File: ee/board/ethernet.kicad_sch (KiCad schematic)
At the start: 20 parts, among them J8 HR911105A, U1 RTL8201F, Y1 Crystal_GND24_Small

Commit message: Nearly finished routing.
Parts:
- removed RN1 (x2): 10k, Resistor_SMD:R_Array_Convex_4x0402, symbol Device:R_Pack04
- added C16: 100nF, Capacitor_SMD:C_0603_1608Metric, symbol Device:C_Small
- added R17 (x7): 5.1k, Resistor_SMD:R_0603_1608Metric, symbol Device:R_Small_US
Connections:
- net +3V3: now also C16.1, R17.2, R17.2, R17.2, R17.2
- net GND: now also C16.2, R17.1, R17.1, R17.1
- net RMII_MDC: now also R17.1
- net RMII_MDIO: now also R17.1
- net RMII_RXD1: now also R17.2
- net RMII_RXER: now also R17.2
- net at U1.12 (CLK_CTL): now also R17.1, R17.2
- net at U1.8 (RXDV): now also R17.1
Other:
- moved on the sheet: C10, C8

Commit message: Finished R1
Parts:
- C10, C11, C12, C16, C8: MPN (none) -> CC0603KRX7R7BB104
- C14, C15: MPN (none) -> CC0603JPNPO9BN180
- R17: MPN (none) -> RC0603FR-135K1L
- R17: MPN (none) -> RC0603FR-13470KL
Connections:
- net GND: now also J8.13 (SHIELD), J8.14 (SHIELD); no longer J8.15 (SHIELD), J8.16 (SHIELD)
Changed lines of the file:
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@@
   (junction (at 86.995 90.17) (diameter 0) (color 0 0 0 0)
+  )
+  (junction (at 190.5 124.46) (diameter 0) (color 0 0 0 0)
   )
   (junction (at 83.185 100.33) (diameter 0) (color 0 0 0 0)
@@
     (stroke (width 0) (type default))
   )
+  (wire (pts (xy 190.5 121.92) (xy 190.5 124.46))
+    (stroke (width 0) (type default))
+  )
   (wire (pts (xy 181.61 92.71) (xy 185.42 92.71))
     (stroke (width 0) (type default))
@@
     (stroke (width 0) (type default))
   )
+  (wire (pts (xy 190.5 124.46) (xy 191.77 124.46))
+    (stroke (width 0) (type default))
+  )
   (wire (pts (xy 137.795 88.265) (xy 145.415 88.265))
     (stroke (width 0) (type default))
@@
     (stroke (width 0) (type default))
   )
-  (wire (pts (xy 190.5 125.095) (xy 190.5 123.19))
+  (wire (pts (xy 190.5 129.54) (xy 190.5 124.46))
     (stroke (width 0) (type default))
   )
@@
     (stroke (width 0) (type default))
   )
+  (wire (pts (xy 191.77 121.92) (xy 190.5 121.92))
+    (stroke (width 0) (type default))
+  )
   (wire (pts (xy 69.215 109.855) (xy 69.215 116.84))
     (stroke (width 0) (type default))
@@
   )
   (wire (pts (xy 137.795 74.295) (xy 145.415 74.295))
-    (stroke (width 0) (type default))
-  )
-  (wire (pts (xy 190.5 123.19) (xy 191.77 123.19))
     (stroke (width 0) (type default))
   )
@@
     (pin "11")
     (pin "12")
-    (pin "15")
-    (pin "16")
     (pin "2")
     (pin "3")
@@
     (pin "8")
     (pin "9")
+    (pin "13")
+    (pin "14")
     (instances
       (project "board"
@@
     )
     (property "Datasheet" "~" (at 173.99 124.46 0)
+      (effects (font (size 1.27 1.27)) hide)
+    )
+    (property "MPN" "RC0603FR-135K1L" (at 173.99 124.46 0)
       (effects (font (size 1.27 1.27)) hide)
     )
@@
     )
   )
-  (symbol (lib_id "power:GND") (at 190.5 125.095 0) (unit 1)
+  (symbol (lib_id "power:GND") (at 190.5 129.54 0) (unit 1)
     (in_bom yes) (on_board yes) (dnp no) (fields_autoplaced)
-    (property "Reference" "#PWR030" (at 190.5 131.445 0)
-      (effects (font (size 1.27 1.27)) hide)
-    )
-    (property "Value" "GND" (at 190.5 129.5384 0)
-      (effects (font (size 1.27 1.27)) hide)
-    )
-    (property "Footprint" "" (at 190.5 125.095 0)
-      (effects (font (size 1.27 1.27)) hide)
-    )
-    (property "Datasheet" "" (at 190.5 125.095 0)
+    (property "Reference" "#PWR030" (at 190.5 135.89 0)
+      (effects (font (size 1.27 1.27)) hide)
+    )
+    (property "Value" "GND" (at 190.5 133.9834 0)
+      (effects (font (size 1.27 1.27)) hide)
+    )
+    (property "Footprint" "" (at 190.5 129.54 0)
+      (effects (font (size 1.27 1.27)) hide)
+    )
+    (property "Datasheet" "" (at 190.5 129.54 0)
       (effects (font (size 1.27 1.27)) hide)
     )
@@
       (effects (font (size 1.27 1.27)) hide)
     )
+    (property "MPN" "CC0603KRX7R7BB104" (at 154.305 40.005 0)
+      (effects (font (size 1.27 1.27)) hide)
+    )
     (pin "1")
     (pin "2")
@@
       (effects (font (size 1.27 1.27)) hide)
     )
+    (property "MPN" "CC0603JPNPO9BN180" (at 154.94 85.09 0)
+      (effects (font (size 1.27 1.27)) hide)
+    )
     (pin "1")
     (pin "2")
@@
     )
     (property "Datasheet" "~" (at 182.245 118.11 0)
+      (effects (font (size 1.27 1.27)) hide)
+    )
+    (property "MPN" "RC0603FR-13470KL" (at 182.245 118.11 90)
       (effects (font (size 1.27 1.27)) hide)
     )
@@
     )
     (property "Datasheet" "~" (at 132.715 40.005 0)
+      (effects (font (size 1.27 1.27)) hide)
+    )
+    (property "MPN" "CC0603KRX7R7BB104" (at 132.715 40.005 0)
       (effects (font (size 1.27 1.27)) hide)
     )
@@
       (effects (font (size 1.27 1.27)) hide)
     )
+    (property "MPN" "RC0603FR-135K1L" (at 128.905 74.93 90)
+      (effects (font (size 1.27 1.27)) hide)
+    )
     (pin "1")
     (pin "2")
@@
     )
     (property "Datasheet" "~" (at 173.99 98.425 0)
+      (effects (font (size 1.27 1.27)) hide)
+    )
+    (property "MPN" "RC0603FR-135K1L" (at 173.99 98.425 0)
       (effects (font (size 1.27 1.27)) hide)
     )
@@
       (effects (font (size 1.27 1.27)) hide)
     )
+    (property "MPN" "RC0603FR-135K1L" (at 92.075 48.895 0)
+      (effects (font (size 1.27 1.27)) hide)
+    )
     (pin "1")
     (pin "2")
@@
       (effects (font (size 1.27 1.27)) hide)
     )
+    (property "MPN" "RC0603FR-135K1L" (at 76.2 48.26 0)
+      (effects (font (size 1.27 1.27)) hide)
+    )
     (pin "1")
     (pin "2")
@@
     )
     (property "Datasheet" "~" (at 130.81 99.695 0)
+      (effects (font (size 1.27 1.27)) hide)
+    )
+    (property "MPN" "CC0603KRX7R7BB104" (at 130.81 99.695 0)
       (effects (font (size 1.27 1.27)) hide)
     )
@@
       (effects (font (size 1.27 1.27)) hide)
     )
+    (property "MPN" "RC0603FR-135K1L" (at 76.2 106.68 0)
+      (effects (font (size 1.27 1.27)) hide)
+    )
     (pin "1")
     (pin "2")
@@
       (effects (font (size 1.27 1.27)) hide)
     )
+    (property "MPN" "CC0603JPNPO9BN180" (at 154.94 77.47 0)
+      (effects (font (size 1.27 1.27)) hide)
+    )
     (pin "1")
     (pin "2")
@@
       (effects (font (size 1.27 1.27)) hide)
     )
+    (property "MPN" "CC0603KRX7R7BB104" (at 142.875 40.005 0)
+      (effects (font (size 1.27 1.27)) hide)
+    )
     (pin "1")
     (pin "2")
@@
     )
     (property "Datasheet" "~" (at 83.185 106.68 0)
+      (effects (font (size 1.27 1.27)) hide)
+    )
+    (property "MPN" "RC0603FR-135K1L" (at 83.185 106.68 0)
       (effects (font (size 1.27 1.27)) hide)
     )
@@
       (effects (font (size 1.27 1.27)) hide)
     )
+    (property "MPN" "RC0603FR-135K1L" (at 69.215 107.315 0)
+      (effects (font (size 1.27 1.27)) hide)
+    )
     (pin "1")
     (pin "2")
@@
     )
     (property "Datasheet" "~" (at 123.825 99.695 0)
+      (effects (font (size 1.27 1.27)) hide)
+    )
+    (property "MPN" "CC0603KRX7R7BB104" (at 123.825 99.695 0)
       (effects (font (size 1.27 1.27)) hide)
     )
@@
       (effects (font (size 1.27 1.27)) hide)
     )
+    (property "MPN" "RC0603FR-135K1L" (at 129.54 134.62 90)
+      (effects (font (size 1.27 1.27)) hide)
+    )
     (pin "1")
     (pin "2")
@@
       (effects (font (size 1.27 1.27)) hide)
     )
+    (property "MPN" "RC0603FR-135K1L" (at 81.28 48.895 0)
+      (effects (font (size 1.27 1.27)) hide)
+    )
     (pin "1")
     (pin "2")
@@
     )
     (property "Datasheet" "~" (at 182.245 105.41 0)
+      (effects (font (size 1.27 1.27)) hide)
+    )
+    (property "MPN" "RC0603FR-13470KL" (at 182.245 105.41 90)
       (effects (font (size 1.27 1.27)) hide)
     )
@@
       (effects (font (size 1.27 1.27)) hide)
     )
+    (property "MPN" "RC0603FR-135K1L" (at 86.995 48.895 0)
+      (effects (font (size 1.27 1.27)) hide)
+    )

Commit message: Changed inductor side in R0.1 to fit the part number.
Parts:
- C13, C18: MPN (none) -> CC0603KRX7R7BB223
- C9: MPN (none) -> CC0603KRX7R7BB102
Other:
- company: (none) -> Interrupt Labs
- title: (none) -> Flipper Blackhat
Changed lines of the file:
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@@
 (kicad_sch (version 20230121) (generator eeschema)
   (paper "A4")
+  (title_block
+    (title "Flipper Blackhat")
+    (date "2024-01-09")
+    (rev "R0.1")
+    (company "Interrupt Labs")
+    (comment 1 "Ryan Walker")
+    (comment 2 "Walker@interruptlabs.ca")
+  )
   (junction (at 185.42 92.71) (diameter 0) (color 0 0 0 0)
   )
@@
     )
     (property "Datasheet" "~" (at 124.46 142.24 0)
+      (effects (font (size 1.27 1.27)) hide)
+    )
+    (property "MPN" "CC0603KRX7R7BB102" (at 124.46 142.24 0)
       (effects (font (size 1.27 1.27)) hide)
     )
@@
       (effects (font (size 1.27 1.27)) hide)
     )
+    (property "MPN" "CC0603KRX7R7BB223" (at 185.42 85.725 0)
+      (effects (font (size 1.27 1.27)) hide)
+    )
     (pin "1")
     (pin "2")
@@
       (effects (font (size 1.27 1.27)) hide)
     )
+    (property "MPN" "CC0603KRX7R7BB223" (at 181.61 85.725 0)
+      (effects (font (size 1.27 1.27)) hide)
+    )

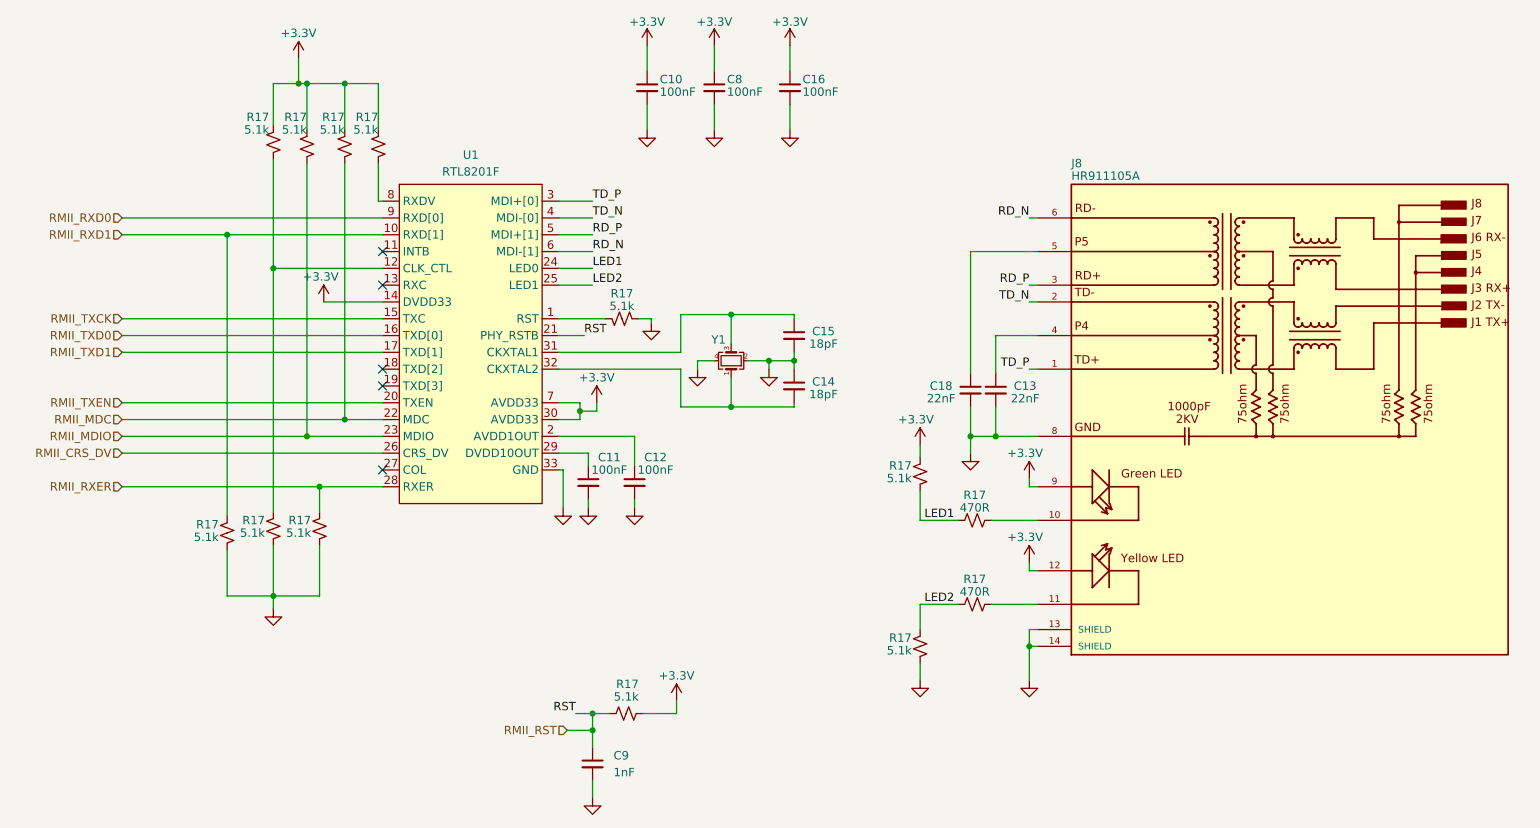
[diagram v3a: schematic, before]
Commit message: Added the footprints into the design.
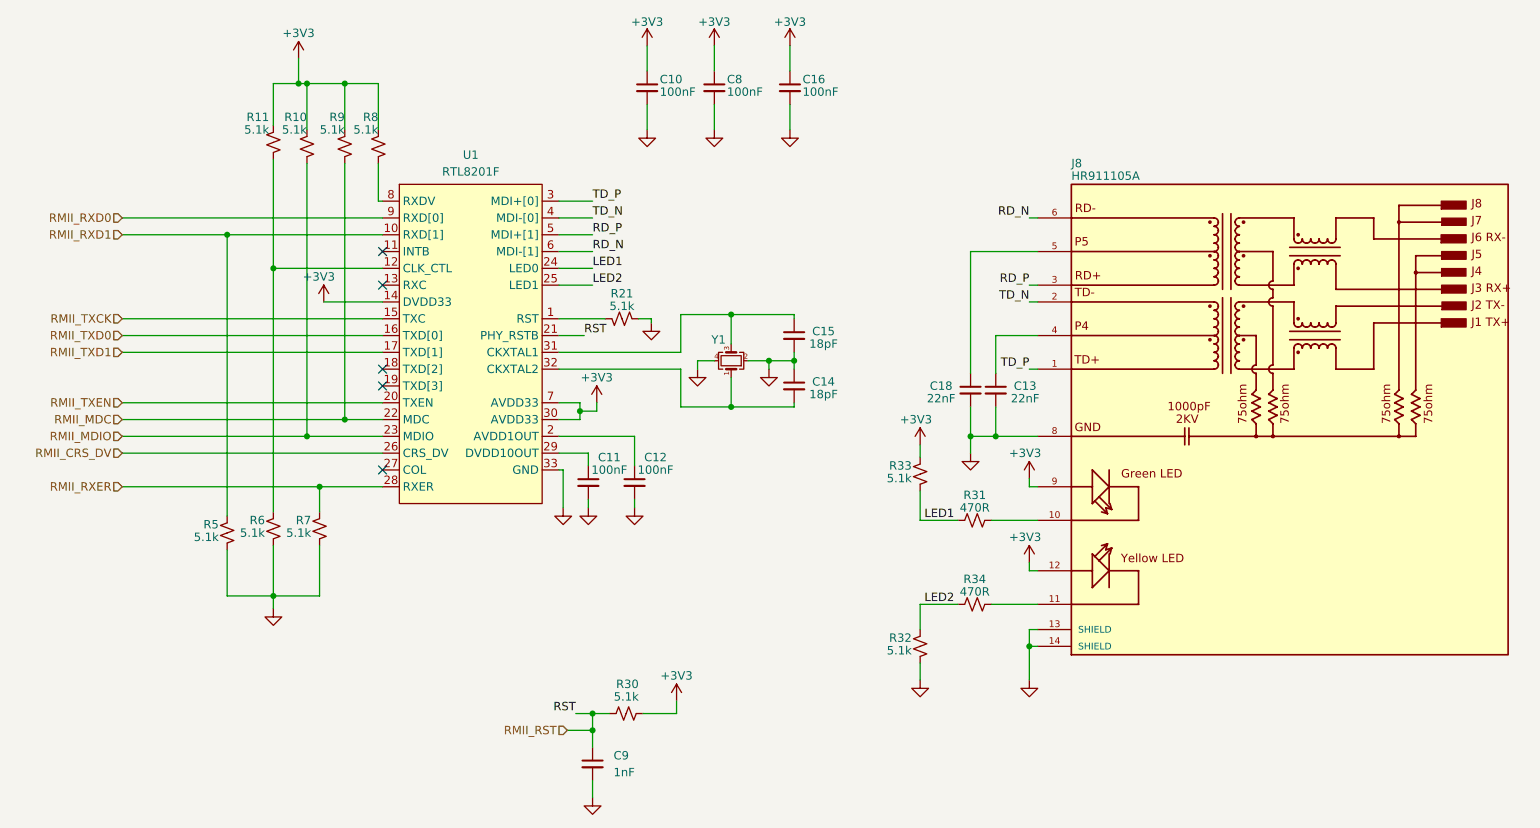
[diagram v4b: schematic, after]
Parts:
- renumbered R17 to R10, R17 to R11, R17 to R21, R17 to R30, R17 to R31, R17 to R32, R17 to R33, R17 to R34, R17 to R5, R17 to R6, R17 to R7, R17 to R8, R17 to R9
